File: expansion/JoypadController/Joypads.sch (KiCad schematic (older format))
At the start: 2 parts

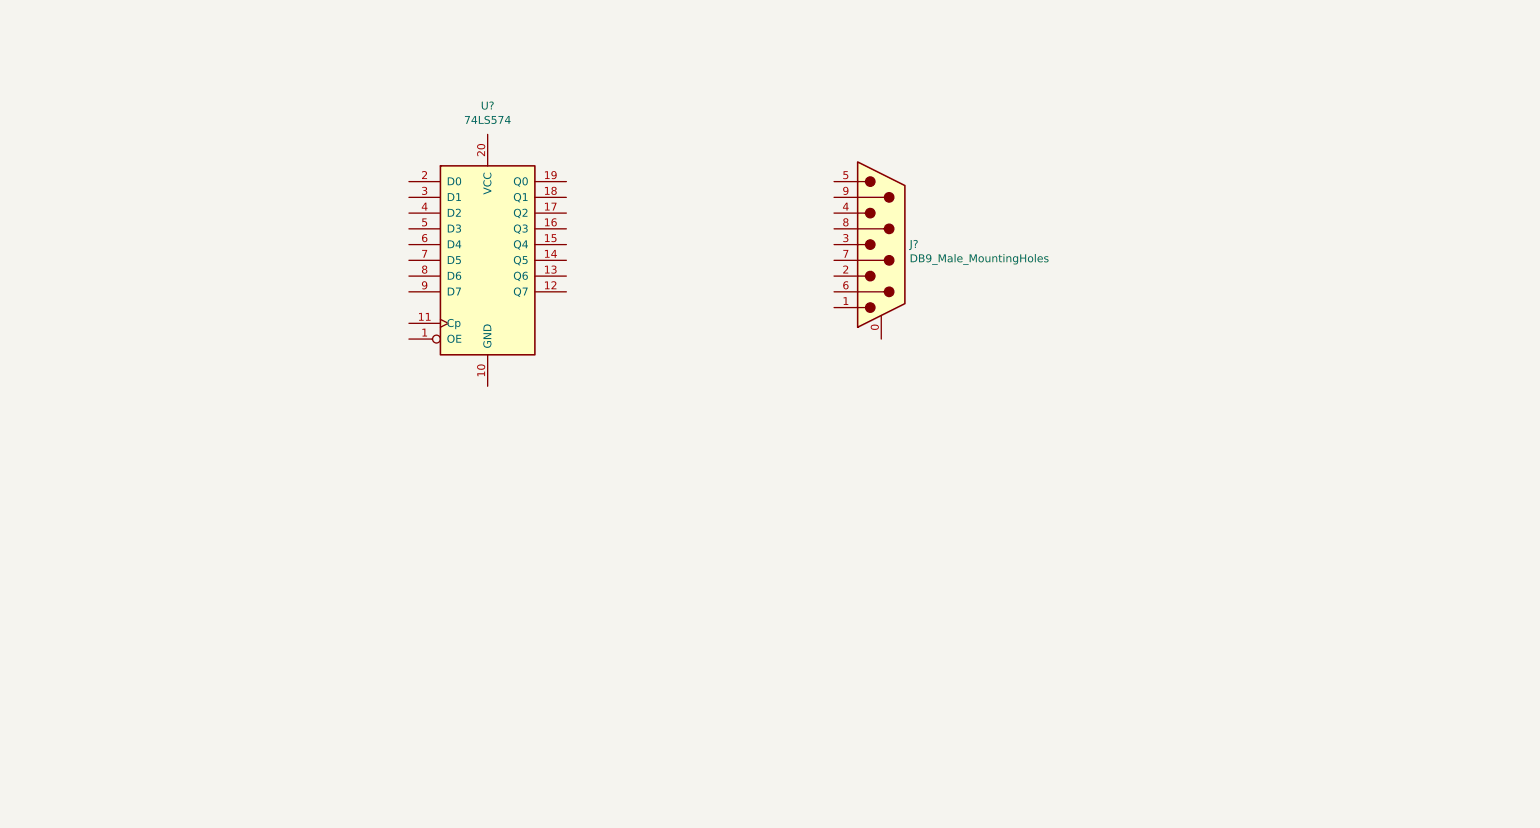
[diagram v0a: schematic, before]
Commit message: Added PCB for Joypad controller
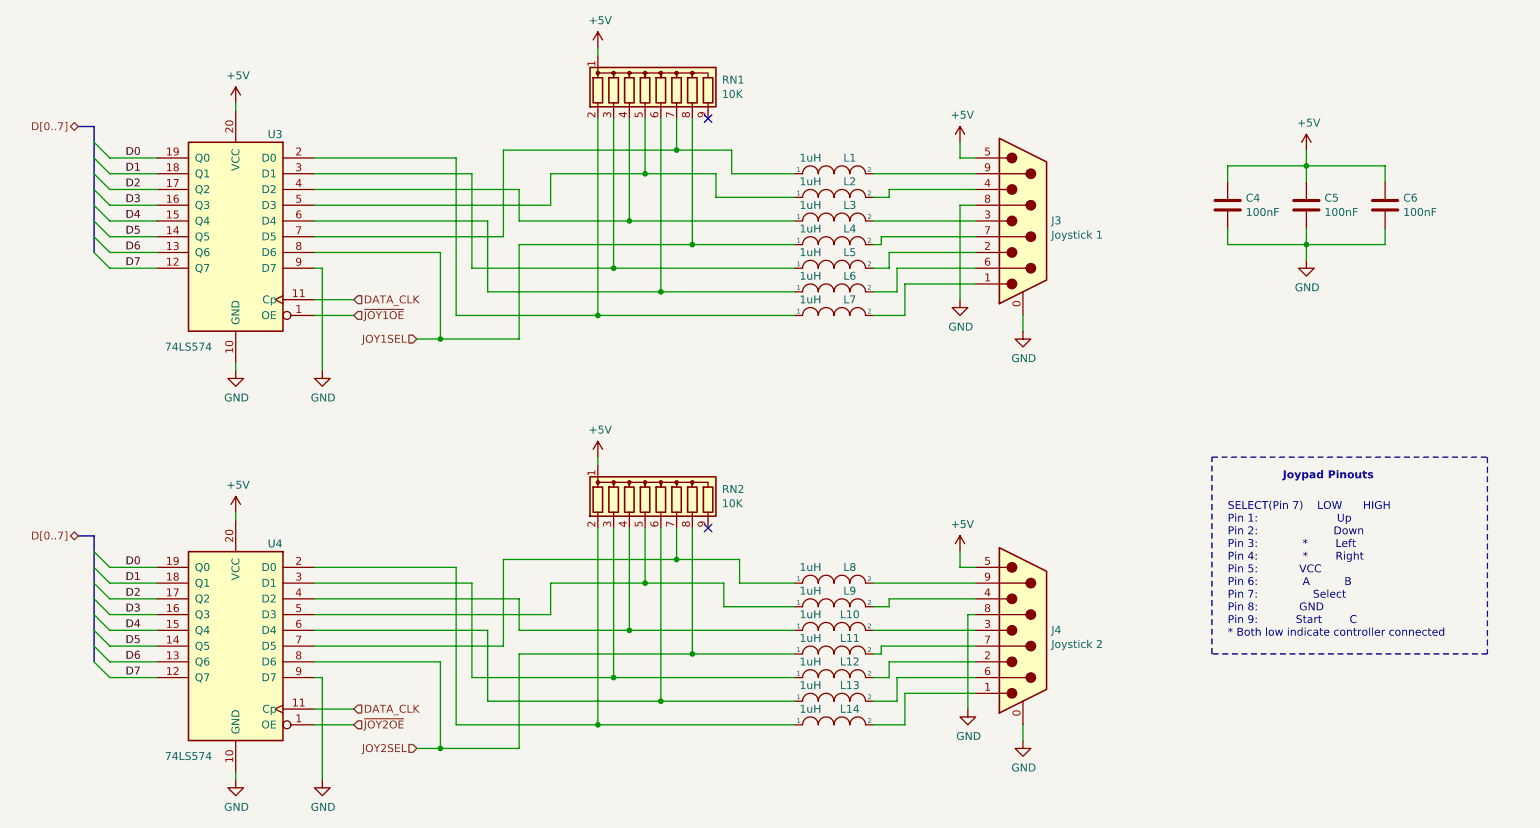
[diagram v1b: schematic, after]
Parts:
- added C4, C5, C6: 100nF, Capacitor_THT:C_Disc_D5.0mm_W2.5mm_P2.50mm, symbol Device:C
- added J4: Joystick 2, Connector_Dsub:DSUB-9_Male_Horizontal_P2.77x2.84mm_EdgePinOffset4.94mm_Housed_MountingHolesOffset7.48mm, symbol Connector:DB9_Male_MountingHoles
- added L1, L10, L11, L12, L13, L14, L2, L3, L4, L5, L6, L7, L8, L9: 1uH, Inductor_THT:L_Axial_L6.6mm_D2.7mm_P10.16mm_Horizontal_Vishay_IM-2, symbol pspice:INDUCTOR
- added RN1, RN2: 10K, Resistor_THT:R_Array_SIP9, symbol Device:R_Network08
- added U4: 74LS574, Package_DIP:DIP-20_W7.62mm_Socket, symbol 74xx:74LS574
- J3: renamed from J?; value DB9_Male_MountingHoles -> Joystick 1; footprint (none) -> Connector_Dsub:DSUB-9_Male_Horizontal_P2.77x2.84mm_EdgePinOffset4.94mm_Housed_MountingHolesOffset7.48mm
- U3: renamed from U?; footprint (none) -> Package_DIP:DIP-20_W7.62mm_Socket
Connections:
- net ~JOY1OE: now reaches U3.1 (OE)
- net GND: now reaches U3.10 (GND)
- net GND: now also J3.0 (PAD), J3.8, U3.9 (D7), C4.2, C5.2, C6.2, J4.0 (PAD), J4.8, U4.10 (GND), U4.9 (D7)
- net DATA_CLK: now reaches U3.11 (Cp)
- net DATA_CLK: now also U4.11 (Cp)
- net D7: now reaches U3.12 (Q7)
- net D7: now also U4.12 (Q7)
- net D6: now reaches U3.13 (Q6)
- net D6: now also U4.13 (Q6)
- net D5: now reaches U3.14 (Q5)
- net D5: now also U4.14 (Q5)
- net D4: now reaches U3.15 (Q4)
- net D4: now also U4.15 (Q4)
- net D3: now reaches U3.16 (Q3)
- net D3: now also U4.16 (Q3)
- net D2: now reaches U3.17 (Q2)
- net D2: now also U4.17 (Q2)
- net D1: now reaches U3.18 (Q1)
- net D1: now also U4.18 (Q1)
- net D0: now reaches U3.19 (Q0)
- net D0: now also U4.19 (Q0)
- net at U3.2 (D0): now also L7.1, RN1.2 (R1)
- net +5V: now reaches U3.20 (VCC)
- net +5V: now also J3.5, C4.1, C5.1, C6.1, J4.5, RN1.1 (common), RN2.1 (common), U4.20 (VCC)
- net at U3.3 (D1): now also L5.1, RN1.3 (R2)
- net at U3.4 (D2): now also L3.1, RN1.4 (R3)
- net at U3.5 (D3): now also L2.1, RN1.5 (R4)
- net at U3.6 (D4): now also L6.1, RN1.6 (R5)
- net at U3.7 (D5): now also L1.1, RN1.7 (R6)
- net JOY1SEL: now reaches U3.8 (D6)
- net JOY1SEL: now also L4.1, RN1.8 (R7)
- net at J3.1: now also L7.2
- net at J3.2: now also L5.2
- net at J3.3: now also L3.2
- net at J3.4: now also L2.2
- net at J3.6: now also L6.2
- net at J3.7: now also L4.2
- net at J3.9: now also L1.2
- new net: J4.1, L14.2
- new net: J4.2, L12.2
- new net: J4.3, L10.2
- new net: J4.4, L9.2
- new net: J4.6, L13.2
- new net: J4.7, L11.2
- new net: J4.9, L8.2
- new net: L14.1, RN2.2 (R1), U4.2 (D0)
- new net: L12.1, RN2.3 (R2), U4.3 (D1)
- new net: L10.1, RN2.4 (R3), U4.4 (D2)
- new net: L9.1, RN2.5 (R4), U4.5 (D3)
- new net: L13.1, RN2.6 (R5), U4.6 (D4)
- new net: L8.1, RN2.7 (R6), U4.7 (D5)
- new net JOY2SEL: L11.1, RN2.8 (R7), U4.8 (D6)
- new net ~JOY2OE: U4.1 (OE)
- no-connect marks 0 -> 2
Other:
- note added: "Joypad Pinouts\n"
- note added: "SELECT(Pin 7) LOW HIGH\nPin 1: Up\nPin 2: Down\nPin 3: * Left\nPin 4: * Right\nPin 5: VCC\nPin 6: A B \nPin 7: Select \nPin 8: GND\nPin 9: Start C\n* Both low indicate controller connected\n"
- moved on the sheet: J3, U3
